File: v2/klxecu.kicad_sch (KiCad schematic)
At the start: 14 parts, among them J1 CAM_SENSOR_IN, J2 Conn_01x06, U1 S36B-WPZK-A, U2 LM2940S-5.0/NOPB, U3 Arduino Mega 2560 Pro

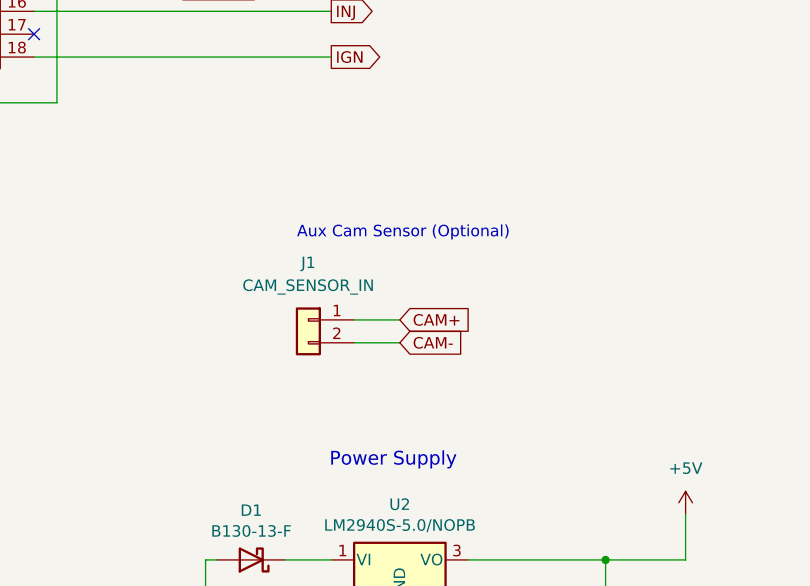
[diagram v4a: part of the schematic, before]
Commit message: add 12v/5v/GND options to cam sensor connector
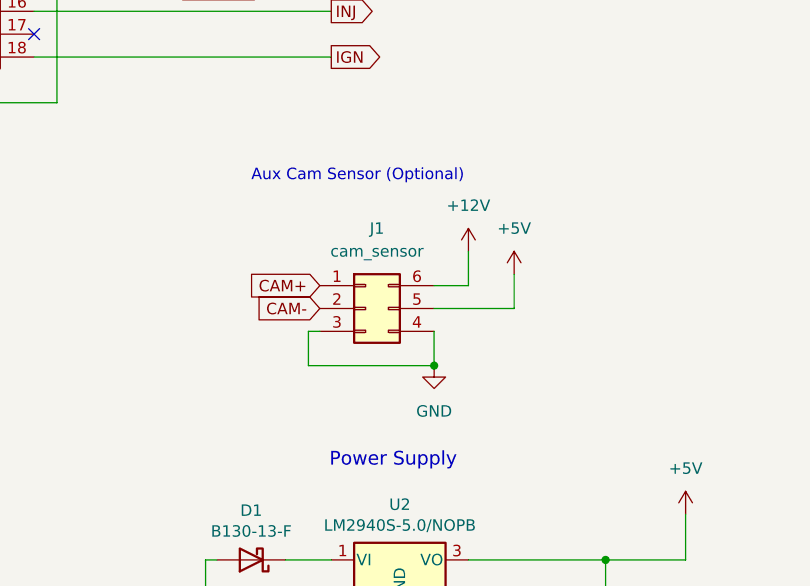
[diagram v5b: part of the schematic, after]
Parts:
- removed J1: CAM_SENSOR_IN, Connector_PinHeader_2.54mm:PinHeader_1x02_P2.54mm_Vertical, symbol Connector_Generic:Conn_01x02
- added J1: cam_sensor, Connector_PinHeader_2.54mm:PinHeader_2x03_P2.54mm_Vertical, symbol Connector_Generic:Conn_02x03_Counter_Clockwise
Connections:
- net +12V: now also J1.6 (Pin_6)
- net +5V: now also J1.5 (Pin_5)
- net CAM+: now also J1.1 (Pin_1)
- net CAM-: now also J1.2 (Pin_2)
- net GND: now also J1.3 (Pin_3), J1.4 (Pin_4)
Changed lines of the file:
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@@
   (junction (at 134.62 132.08) (diameter 0) (color 0 0 0 0)
+  )
+  (junction (at 115.57 110.49) (diameter 0) (color 0 0 0 0)
   )
   (junction (at 125.73 148.59) (diameter 0) (color 0 0 0 0)
@@
     (stroke (width 0) (type default) (color 0 0 0 0))
   )
+  (wire (pts (xy 101.6 110.49) (xy 115.57 110.49))
+    (stroke (width 0) (type default) (color 0 0 0 0))
+  )
   (wire (pts (xy 34.29 63.5) (xy 58.42 63.5))
     (stroke (width 0) (type default) (color 0 0 0 0))
@@
     (stroke (width 0) (type default) (color 0 0 0 0))
   )
+  (wire (pts (xy 115.57 106.68) (xy 115.57 110.49))
+    (stroke (width 0) (type default) (color 0 0 0 0))
+  )
   (wire (pts (xy 81.28 25.4) (xy 81.28 63.5))
     (stroke (width 0) (type default) (color 0 0 0 0))
@@
     (stroke (width 0) (type default) (color 0 0 0 0))
   )
+  (wire (pts (xy 115.57 101.6) (xy 119.38 101.6))
+    (stroke (width 0) (type default) (color 0 0 0 0))
+  )
   (wire (pts (xy 78.74 148.59) (xy 90.17 148.59))
     (stroke (width 0) (type default) (color 0 0 0 0))
@@
     (stroke (width 0) (type default) (color 0 0 0 0))
   )
+  (wire (pts (xy 101.6 106.68) (xy 101.6 110.49))
+    (stroke (width 0) (type default) (color 0 0 0 0))
+  )
   (wire (pts (xy 78.74 146.05) (xy 78.74 148.59))
     (stroke (width 0) (type default) (color 0 0 0 0))
@@
     (stroke (width 0) (type default) (color 0 0 0 0))
   )
-  (wire (pts (xy 106.68 105.41) (xy 111.76 105.41))
-    (stroke (width 0) (type default) (color 0 0 0 0))
-  )
   (wire (pts (xy 64.77 148.59) (xy 78.74 148.59))
     (stroke (width 0) (type default) (color 0 0 0 0))
@@
     (stroke (width 0) (type default) (color 0 0 0 0))
   )
-  (wire (pts (xy 106.68 107.95) (xy 111.76 107.95))
-    (stroke (width 0) (type default) (color 0 0 0 0))
-  )
   (wire (pts (xy 125.73 148.59) (xy 111.76 148.59))
     (stroke (width 0) (type default) (color 0 0 0 0))
@@
     (stroke (width 0) (type default) (color 0 0 0 0))
   )
+  (wire (pts (xy 124.46 100.33) (xy 124.46 104.14))
+    (stroke (width 0) (type default) (color 0 0 0 0))
+  )
   (wire (pts (xy 71.12 45.72) (xy 87.63 45.72))
     (stroke (width 0) (type default) (color 0 0 0 0))
@@
     (stroke (width 0) (type default) (color 0 0 0 0))
   )
+  (wire (pts (xy 101.6 106.68) (xy 102.87 106.68))
+    (stroke (width 0) (type default) (color 0 0 0 0))
+  )
+  (wire (pts (xy 119.38 101.6) (xy 119.38 97.79))
+    (stroke (width 0) (type default) (color 0 0 0 0))
+  )
   (wire (pts (xy 71.12 68.58) (xy 87.63 68.58))
     (stroke (width 0) (type default) (color 0 0 0 0))
@@
     (stroke (width 0) (type default) (color 0 0 0 0))
   )
+  (wire (pts (xy 124.46 104.14) (xy 115.57 104.14))
+    (stroke (width 0) (type default) (color 0 0 0 0))
+  )
   (wire (pts (xy 55.88 138.43) (xy 64.77 138.43))
     (stroke (width 0) (type default) (color 0 0 0 0))
@@
     (stroke (width 0) (type default) (color 0 0 0 0))
   )
-  (text "Aux Cam Sensor (Optional)\n" (at 100.33 96.52 0)
+  (text "Aux Cam Sensor (Optional)\n" (at 95.25 90.17 0)
     (effects (font (size 1.27 1.27)) (justify left bottom))
   )
@@
     )
   )
-  (global_label "CAM+" (shape input) (at 111.76 105.41 0) (fields_autoplaced)
-    (effects (font (size 1.27 1.27)) (justify left))
-    (property "Intersheet References" "${INTERSHEET_REFS}" (id 0) (at 119.5555 105.3306 0)
-      (effects (font (size 1.27 1.27)) (justify left) hide)
+  (global_label "CAM+" (shape input) (at 102.87 101.6 180) (fields_autoplaced)
+    (effects (font (size 1.27 1.27)) (justify right))
+    (property "Intersheet References" "${INTERSHEET_REFS}" (id 0) (at 95.0745 101.6794 0)
+      (effects (font (size 1.27 1.27)) (justify right) hide)
     )
   )
@@
     )
   )
-  (global_label "CAM-" (shape input) (at 111.76 107.95 0) (fields_autoplaced)
-    (effects (font (size 1.27 1.27)) (justify left))
-    (property "Intersheet References" "${INTERSHEET_REFS}" (id 0) (at 119.5555 107.8706 0)
-      (effects (font (size 1.27 1.27)) (justify left) hide)
+  (global_label "CAM-" (shape input) (at 102.87 104.14 180) (fields_autoplaced)
+    (effects (font (size 1.27 1.27)) (justify right))
+    (property "Intersheet References" "${INTERSHEET_REFS}" (id 0) (at 95.0745 104.2194 0)
+      (effects (font (size 1.27 1.27)) (justify right) hide)
     )
   )
@@
     (pin "1")
     (pin "2")
+  )
+  (symbol (lib_id "power:+12V") (at 119.38 97.79 0) (unit 1)
+    (in_bom yes) (on_board yes) (fields_autoplaced)
+    (property "Reference" "#PWR050" (id 0) (at 119.38 101.6 0)
+      (effects (font (size 1.27 1.27)) hide)
+    )
+    (property "Value" "+12V" (id 1) (at 119.38 92.71 0))
+    (property "Footprint" "" (id 2) (at 119.38 97.79 0)
+      (effects (font (size 1.27 1.27)) hide)
+    )
+    (property "Datasheet" "" (id 3) (at 119.38 97.79 0)
+      (effects (font (size 1.27 1.27)) hide)
+    )
+    (pin "1")
   )
   (symbol (lib_id "Device:CP1") (at 134.62 142.24 0) (unit 1)
@@
     (pin "1")
   )
+  (symbol (lib_id "Connector_Generic:Conn_02x03_Counter_Clockwise") (at 107.95 104.14 0) (unit 1)
+    (in_bom yes) (on_board yes) (fields_autoplaced)
+    (property "Reference" "J1" (id 0) (at 109.22 95.25 0))
+    (property "Value" "cam_sensor" (id 1) (at 109.22 97.79 0))
+    (property "Footprint" "Connector_PinHeader_2.54mm:PinHeader_2x03_P2.54mm_Vertical" (id 2) (at 107.95 104.14 0)
+      (effects (font (size 1.27 1.27)) hide)
+    )
+    (property "Datasheet" "~" (id 3) (at 107.95 104.14 0)
+      (effects (font (size 1.27 1.27)) hide)
+    )
+    (pin "1")
+    (pin "2")
+    (pin "3")
+    (pin "4")
+    (pin "5")
+    (pin "6")
+  )
   (symbol (lib_id "Device:CP1") (at 78.74 142.24 0) (unit 1)
     (in_bom yes) (on_board yes)
@@
     (pin "1")
     (pin "2")
+  )
+  (symbol (lib_id "power:GND") (at 115.57 110.49 0) (unit 1)
+    (in_bom yes) (on_board yes) (fields_autoplaced)
+    (property "Reference" "#PWR049" (id 0) (at 115.57 116.84 0)
+      (effects (font (size 1.27 1.27)) hide)
+    )
+    (property "Value" "GND" (id 1) (at 115.57 115.57 0))
+    (property "Footprint" "" (id 2) (at 115.57 110.49 0)
+      (effects (font (size 1.27 1.27)) hide)
+    )
+    (property "Datasheet" "" (id 3) (at 115.57 110.49 0)
+      (effects (font (size 1.27 1.27)) hide)
+    )
+    (pin "1")
   )
   (symbol (lib_id "power:+5V") (at 215.9 142.24 270) (unit 1)
@@
     (pin "1")
   )
+  (symbol (lib_id "power:+5V") (at 124.46 100.33 0) (unit 1)
+    (in_bom yes) (on_board yes) (fields_autoplaced)
+    (property "Reference" "#PWR051" (id 0) (at 124.46 104.14 0)
+      (effects (font (size 1.27 1.27)) hide)
+    )
+    (property "Value" "+5V" (id 1) (at 124.46 95.25 0))
+    (property "Footprint" "" (id 2) (at 124.46 100.33 0)
+      (effects (font (size 1.27 1.27)) hide)
+    )
+    (property "Datasheet" "" (id 3) (at 124.46 100.33 0)
+      (effects (font (size 1.27 1.27)) hide)
+    )
+    (pin "1")
+  )
   (symbol (lib_id "Device:R") (at 215.9 128.27 180) (unit 1)
     (in_bom yes) (on_board yes)
@@
     (pin "2")
     (pin "3")
-  )
-  (symbol (lib_id "Connector_Generic:Conn_01x02") (at 101.6 105.41 0) (mirror y) (unit 1)
-    (in_bom yes) (on_board yes)
-    (property "Reference" "J1" (id 0) (at 101.6 99.06 0))
-    (property "Value" "CAM_SENSOR_IN" (id 1) (at 101.6 101.6 0))
-    (property "Footprint" "Connector_PinHeader_2.54mm:PinHeader_1x02_P2.54mm_Vertical" (id 2) (at 101.6 105.41 0)
-      (effects (font (size 1.27 1.27)) hide)
-    )
-    (property "Datasheet" "~" (id 3) (at 101.6 105.41 0)
-      (effects (font (size 1.27 1.27)) hide)
-    )
-    (pin "1")
-    (pin "2")
   )
   (symbol (lib_id "mega_2560:mega_2560_pro") (at 142.24 85.09 0) (unit 1)
@@
       (reference "#PWR048") (unit 1) (value "GND") (footprint "")
     )
+    (path "/7c16e2d9-6745-458b-99f5-4d8234d17449"
+      (reference "#PWR049") (unit 1) (value "GND") (footprint "")
+    )
+    (path "/2d615fcf-c993-47f4-8b56-ddee2e407283"
+      (reference "#PWR050") (unit 1) (value "+12V") (footprint "")
+    )
+    (path "/922de356-c4bd-42c2-890f-69db0a32d48c"
+      (reference "#PWR051") (unit 1) (value "+5V") (footprint "")
+    )
     (path "/a01c941e-2669-451e-92d9-4d3556674fec/75126fec-323d-4a00-8d28-b0141aa312d7"
       (reference "A1") (unit 1) (value "Pololu_Breakout_A4988") (footprint "Module:Pololu_Breakout-16_15.2x20.3mm")
@@
       (reference "IC1") (unit 1) (value "SP721") (footprint "Package_DIP:DIP-8_W7.62mm")
     )
-    (path "/b5b28d84-256f-4316-8ca3-297e4f901902"
-      (reference "J1") (unit 1) (value "CAM_SENSOR_IN") (footprint "Connector_PinHeader_2.54mm:PinHeader_1x02_P2.54mm_Vertical")
+    (path "/6b5c12aa-d5cb-4554-b94a-573f41426791"
+      (reference "J1") (unit 1) (value "cam_sensor") (footprint "Connector_PinHeader_2.54mm:PinHeader_2x03_P2.54mm_Vertical")
     )
     (path "/31a8ba14-c84f-4a28-b759-06fbdb564728"
